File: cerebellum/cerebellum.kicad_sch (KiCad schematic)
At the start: 72 parts, among them J1 PowerIn, J2 UART, J3 SWD_DBG, J4 SWD_DBG_PIN, J5 CAN FD, J6 CAN, Q1 AP2300, U1 OK1061-S, U2 AMS1117-3.3, U3 BMI088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

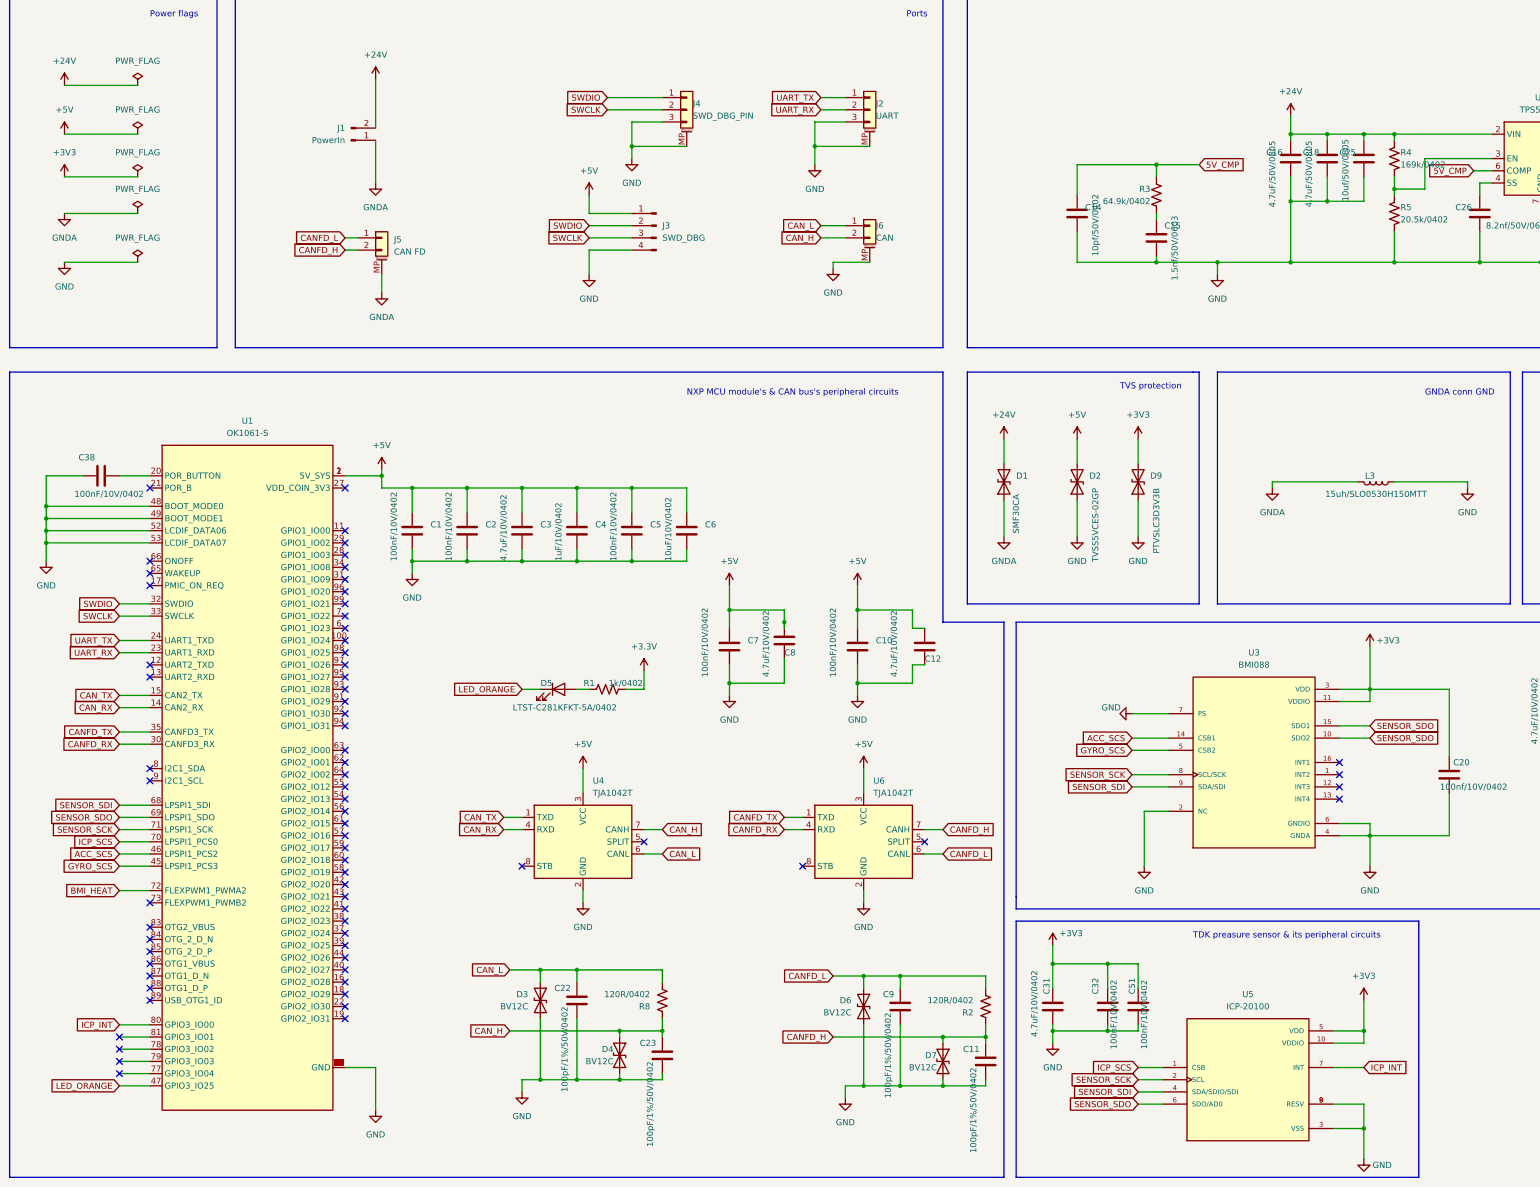
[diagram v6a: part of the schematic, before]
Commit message: [Modify] Change pressure sensor to MPL3115A2R1
Signed-off-by: Homalozoa <nx.tardis@gmail.com>
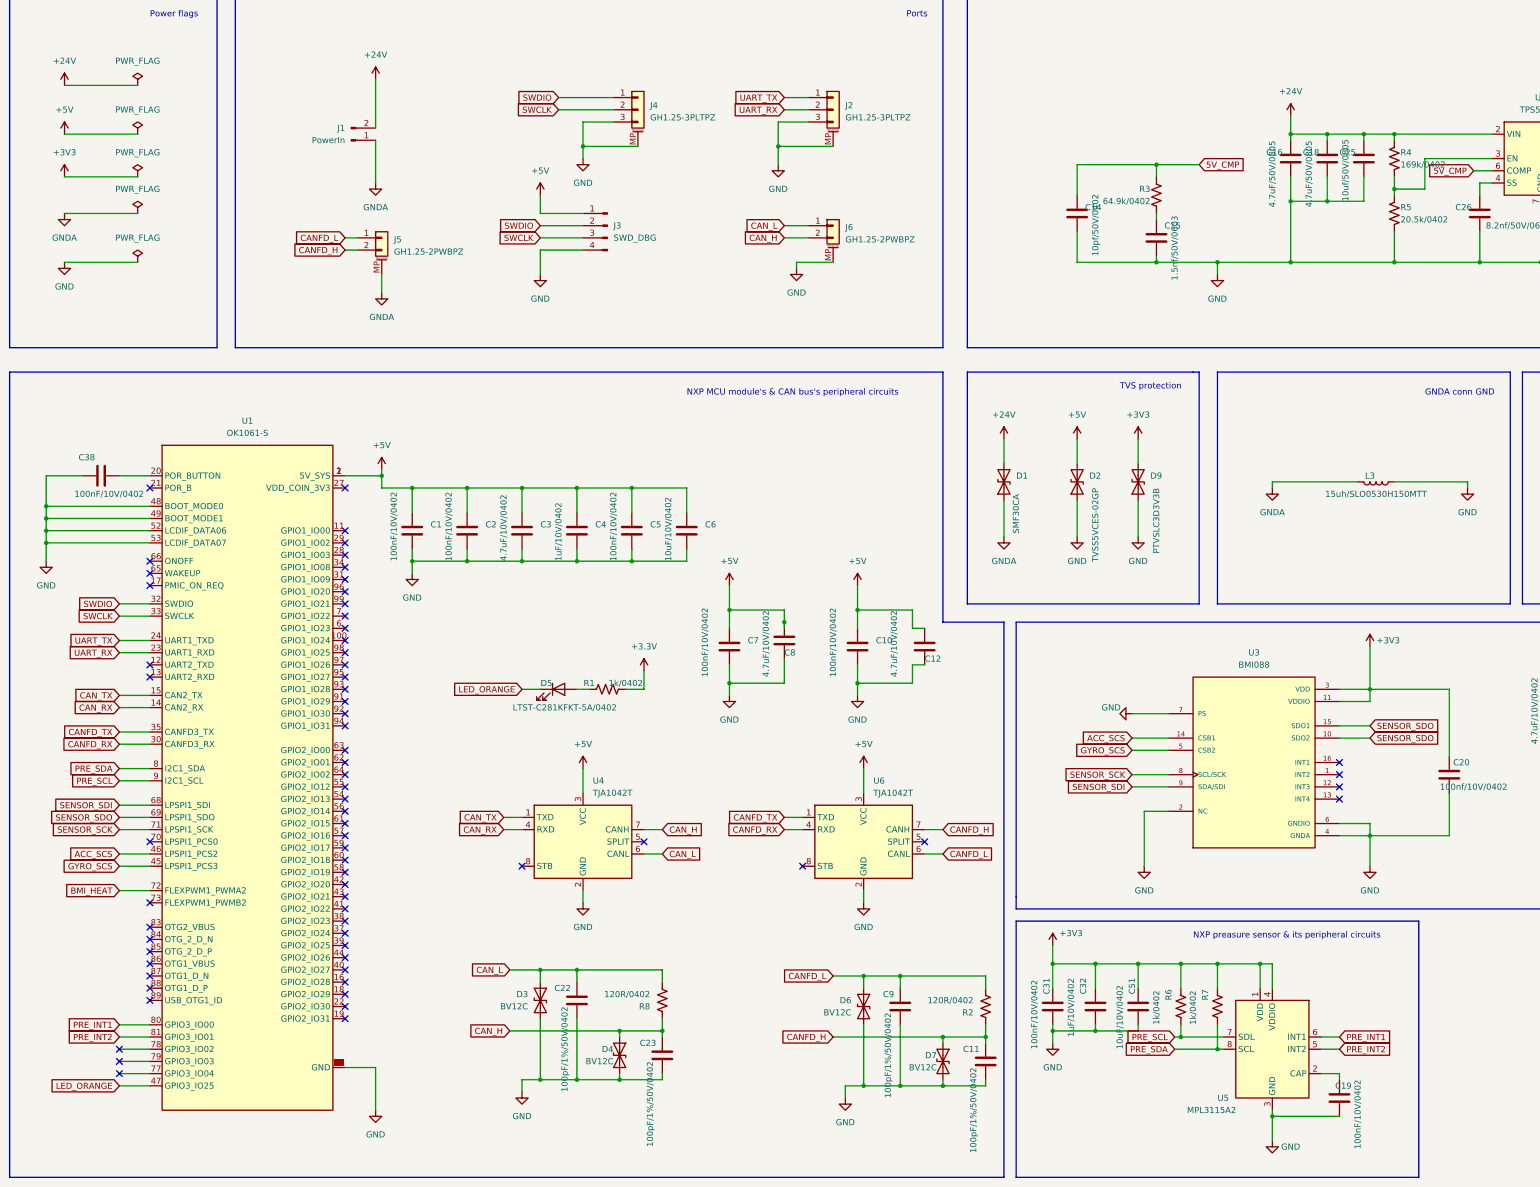
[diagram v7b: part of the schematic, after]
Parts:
- removed U5: ICP-20100, Rolling_Custom:PQFN50P200X200X85-10N, symbol Rolling_Custom:ICP-20100
- added C19: 100nF/10V/0402, Capacitor_SMD:C_0402_1005Metric, symbol Device:C
- added R6, R7: 1k/0402, Resistor_SMD:R_0402_1005Metric, symbol Device:R_US
- added U5: MPL3115A2, Package_LGA:NXP_LGA-8_3x5mm_P1.25mm_H1.1mm, symbol Sensor_Pressure:MPL3115A2
- C31: value 4.7uF/10V/0402 -> 100nF/10V/0402
- C32: value 100nF/10V/0402 -> 1uF/10V/0402
- C51: value 100nF/10V/0402 -> 10uF/10V/0402
- J2: value UART -> GH1.25-3PLTPZ
- J4: value SWD_DBG_PIN -> GH1.25-3PLTPZ
- J5: value CAN FD -> GH1.25-2PWBPZ
- J6: value CAN -> GH1.25-2PWBPZ
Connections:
- net +3V3: now also R6.1, R7.1, U5.1 (VDD), U5.4 (VDDIO)
- net GND: now also C19.1, U5.3 (GND)
- net PRE_SDA: now reaches U1.8 (I2C1_SDA)
- net PRE_SDA: now also R7.2, U5.8 (SCL)
- net PRE_INT2: now reaches U1.81 (GPIO3_IO01)
- net PRE_INT2: now also U5.5 (INT2)
- net PRE_SCL: now reaches U1.9 (I2C1_SCL)
- net PRE_SCL: now also R6.2, U5.7 (SDL)
- net ICP_INT renamed PRE_INT1
- net PRE_INT1: now also U5.6 (INT1)
- net ICP_SCS: no longer names the net of U1.70 (LPSPI1_PCS0)
- new net: C19.2, U5.2 (CAP)
- no-connect marks 69 -> 67
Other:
- note added: "NXP preasure sensor & its peripheral circuits"
- note removed: "TDK preasure sensor & its peripheral circuits"
- moved on the sheet: C32, J2, J3, J4, J6
